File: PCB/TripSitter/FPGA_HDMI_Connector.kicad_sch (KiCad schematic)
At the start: 16 parts, among them J4 HDMI_A_1.4, U12 TPD12S520DBT

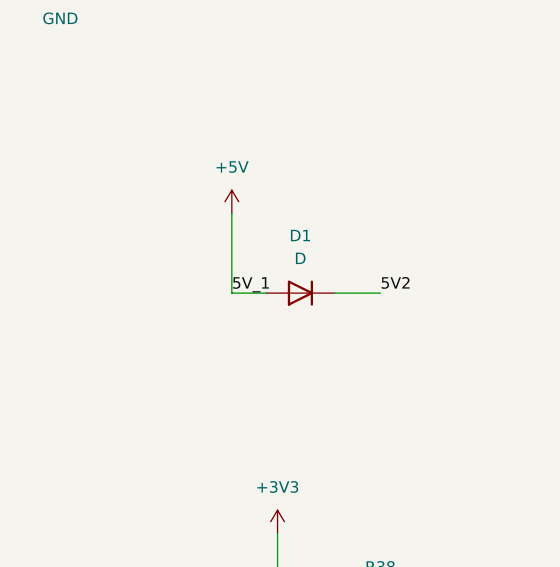
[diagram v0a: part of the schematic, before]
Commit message: add missing tracks on hdmi
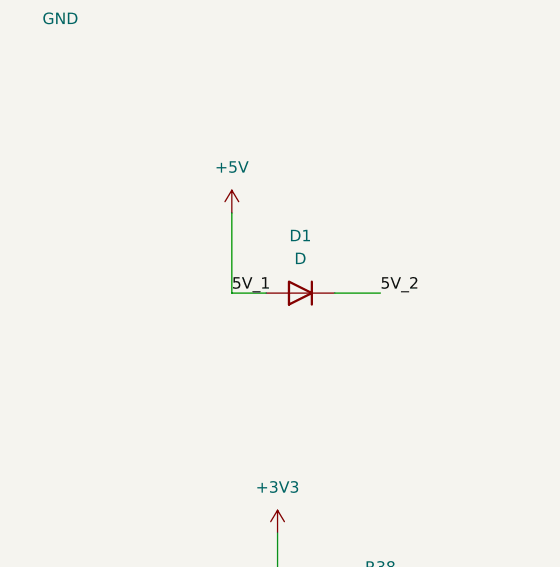
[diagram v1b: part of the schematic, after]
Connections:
- net +5V: no longer D1.1 (K)
- net 5V_2: now also D1.1 (K)
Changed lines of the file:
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@@
     (effects (font (size 1.27 1.27)) (justify left bottom))
   )
-  (label "5V2" (at 261.62 142.24 0) (fields_autoplaced)
+  (label "5V_2" (at 261.62 142.24 0) (fields_autoplaced)
     (effects (font (size 1.27 1.27)) (justify left bottom))
   )
